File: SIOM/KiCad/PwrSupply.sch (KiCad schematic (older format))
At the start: 25 parts, among them J401 24V, U401 LM2594M-12, U402 LM2594M-5.0, U403 LM2594M-3.3

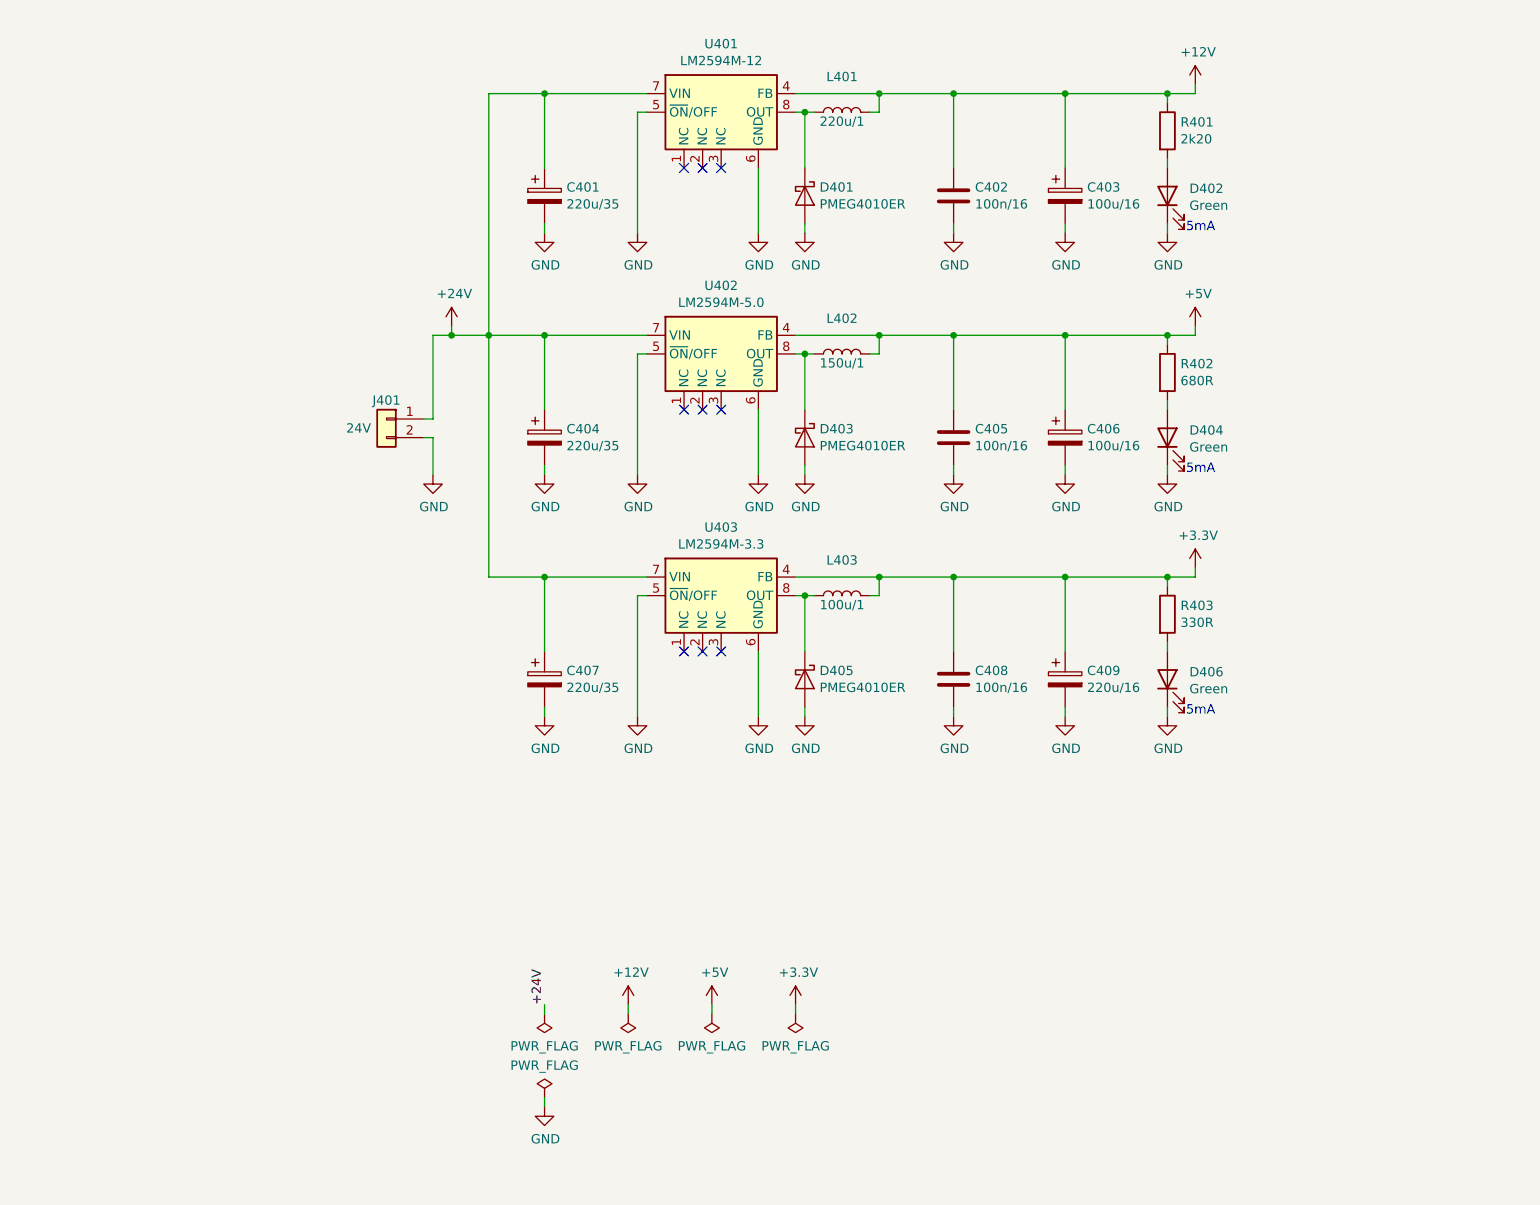
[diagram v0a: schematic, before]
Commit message: KiCad files SIOM_def
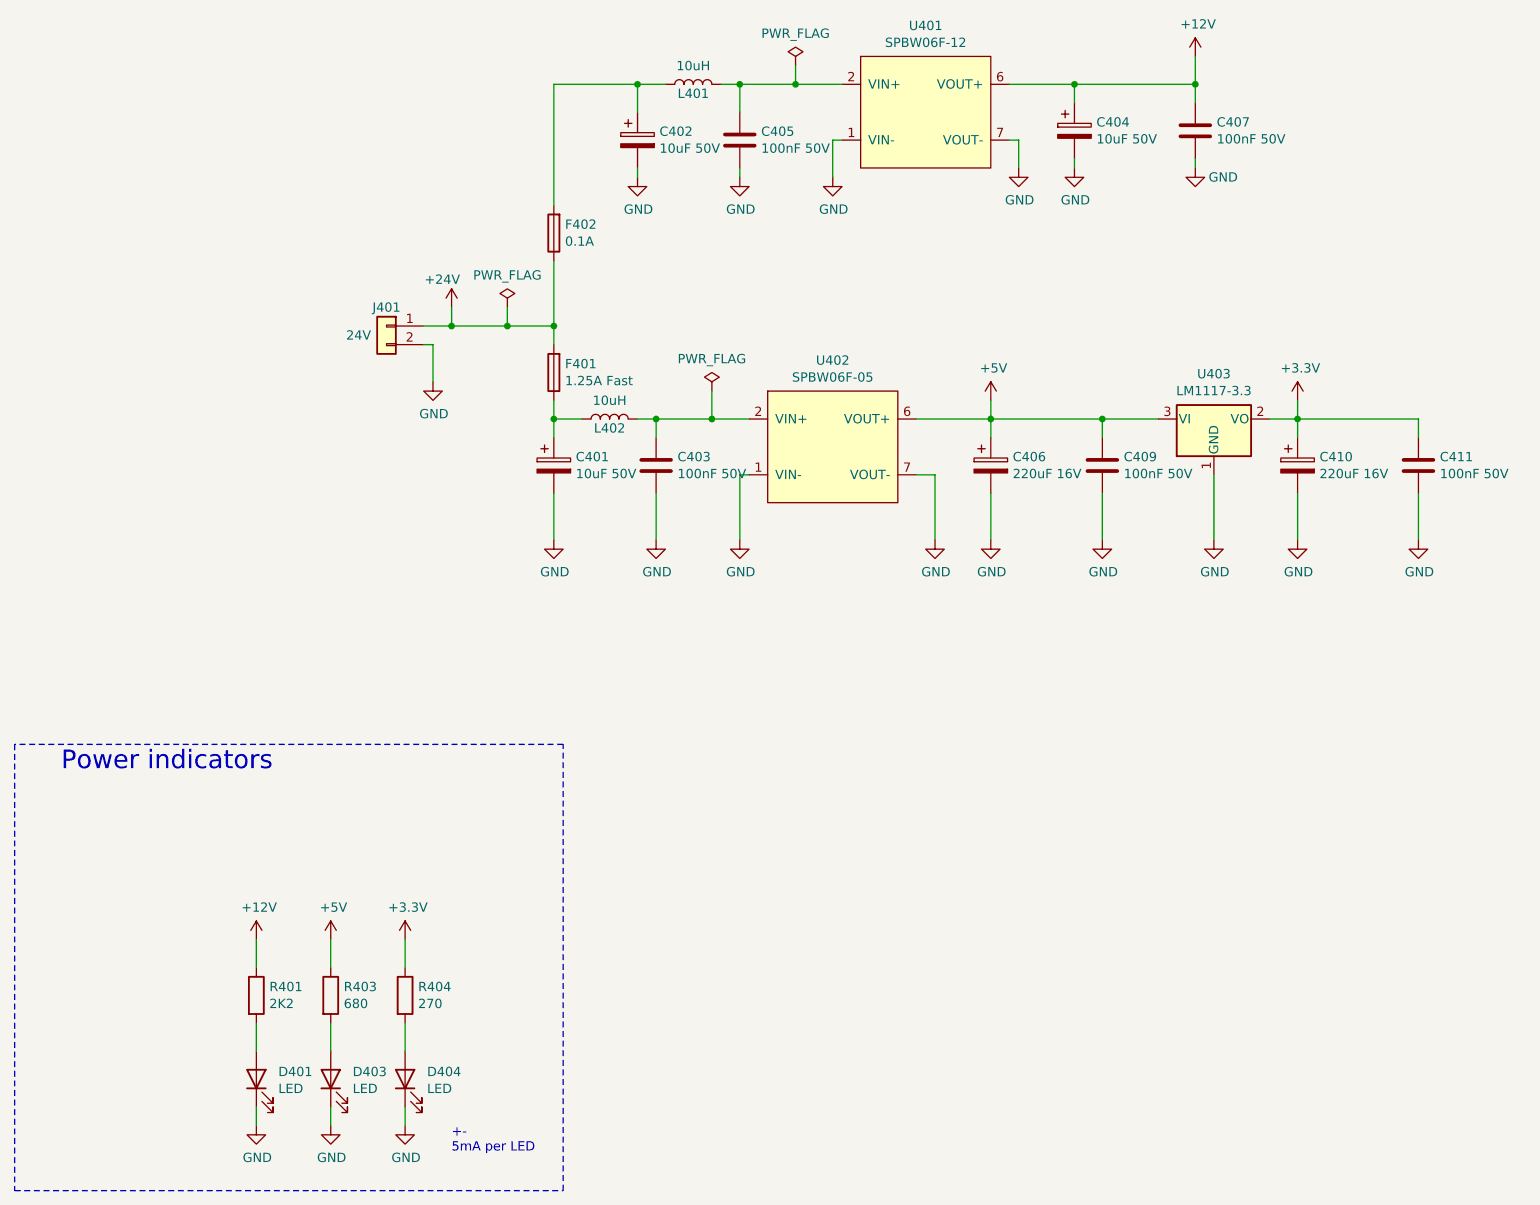
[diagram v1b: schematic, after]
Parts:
- removed C401, C404, C407: 220u/35, Capacitor_SMD:CP_Elec_8x10, symbol SIOMv01-rescue:C_Polarized-Device
- removed C402, C405, C408: 100n/16, Capacitor_SMD:C_0603_1608Metric, symbol SIOMv01-rescue:C-Device
- removed C403, C406: 100u/16, Capacitor_SMD:CP_Elec_8x10, symbol SIOMv01-rescue:C_Polarized-Device
- removed C409: 220u/16, Capacitor_SMD:CP_Elec_8x10, symbol SIOMv01-rescue:C_Polarized-Device
- removed D401, D403, D405: PMEG4010ER, Diode_SMD:Nexperia_CFP3_SOD-123W, symbol SIOMv01-rescue:PMEG4010ER-Diode
- removed D402, D404, D406: Green, LED_SMD:LED_0603_1608Metric, symbol SIOMv01-rescue:LED-Device
- removed L401: 220u/1, Inductor_SMD:L_10.4x10.4_H4.8, symbol SIOMv01-rescue:L-Device
- removed L402: 150u/1, Inductor_SMD:L_10.4x10.4_H4.8, symbol SIOMv01-rescue:L-Device
- removed L403: 100u/1, Inductor_SMD:L_10.4x10.4_H4.8, symbol SIOMv01-rescue:L-Device
- removed R401: 2k20, Resistor_SMD:R_0603_1608Metric, symbol SIOMv01-rescue:R-Device
- removed R402: 680R, Resistor_SMD:R_0603_1608Metric, symbol SIOMv01-rescue:R-Device
- removed R403: 330R, Resistor_SMD:R_0603_1608Metric, symbol SIOMv01-rescue:R-Device
- removed U401: LM2594M-12, Package_SO:SOIC-8_3.9x4.9mm_P1.27mm, symbol SIOMv01-rescue:LM2594M-12-Regulator_Switching
- removed U402: LM2594M-5.0, Package_SO:SOIC-8_3.9x4.9mm_P1.27mm, symbol SIOMv01-rescue:LM2594M-5.0-Regulator_Switching
- removed U403: LM2594M-3.3, Package_SO:SOIC-8_3.9x4.9mm_P1.27mm, symbol SIOMv01-rescue:LM2594M-3.3-Regulator_Switching
- added C401, C402, C404: 10uF 50V, Capacitor_SMD:CP_Elec_5x5.3, symbol Device:CP
- added C403, C405, C407, C409, C411: 100nF 50V, Capacitor_SMD:C_0603_1608Metric, symbol Device:C
- added C406, C410: 220uF 16V, Capacitor_SMD:CP_Elec_6.3x5.8, symbol Device:CP
- added D401, D403, D404: LED, LED_SMD:LED_0805_2012Metric, symbol Device:LED
- added F401: 1.25A Fast, Fuse:Fuse_2920_7451Metric, symbol Device:Fuse
- added F402: 0.1A, Fuse:Fuse_1206_3216Metric_Pad1.42x1.75mm_HandSolder, symbol Device:Fuse
- added L401, L402: 10uH, Inductor_SMD:L_Coilcraft_LPS5030, symbol Device:L
- added R401: 2K2, Resistor_SMD:R_0603_1608Metric, symbol Device:R
- added R403: 680, Resistor_SMD:R_0603_1608Metric, symbol Device:R
- added R404: 270, Resistor_SMD:R_0603_1608Metric, symbol Device:R
- added U401: SPBW06F-12, FTSH:SPAN02, symbol SPBW06:SPBW06F-05
- added U402: SPBW06F-05, FTSH:SPAN02, symbol SPBW06:SPBW06F-05
- added U403: LM1117-3.3, Package_TO_SOT_SMD:SOT-223-3_TabPin2, symbol Regulator_Linear:LM1117-3.3
- J401: footprint TerminalBlock:TerminalBlock_bornier-2_P5.08mm -> Connector_Phoenix_MC:PhoenixContact_MCV_1,5_2-G-3.81_1x02_P3.81mm_Vertical
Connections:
- net +12V: now also C404.1, C407.2, R401.1, U401.6 (VOUT+)
- net +24V: now also F401.2, F402.1
- net +3V3: now also C410.1, C411.2, R404.1, U403.2 (VO)
- net +5V: now also C406.1, C409.2, R403.1, U402.6 (VOUT+), U403.3 (VI)
- net GND: now also C401.2, C402.2, C403.1, C404.2, C405.1, C406.2, C407.1, C409.1, C410.2, C411.1, D401.1 (K), D403.1 (K), D404.1 (K), U401.1 (VIN-), U401.7 (VOUT-), U402.1 (VIN-), U402.7 (VOUT-), U403.1 (GND)
- new net: C402.1, F402.2, L401.1
- new net: C403.2, L402.2, U402.2 (VIN+)
- new net: C405.2, L401.2, U401.2 (VIN+)
- new net: C401.1, F401.1, L402.1
- new net: D401.2 (A), R401.2
- new net: D403.2 (A), R403.2
- new net: D404.2 (A), R404.2
- no-connect marks 9 -> 0
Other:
- note added: "+-\n5mA per LED"
- note added: "Power indicators"
- note removed: "5mA"
- moved on the sheet: J401
